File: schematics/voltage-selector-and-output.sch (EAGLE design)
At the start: 31 parts, among them IC1 5V, IC2 MIC2941, IC3 MCP41010P, IC5 12V, IC6 ATTINY85, Q1 2N3906

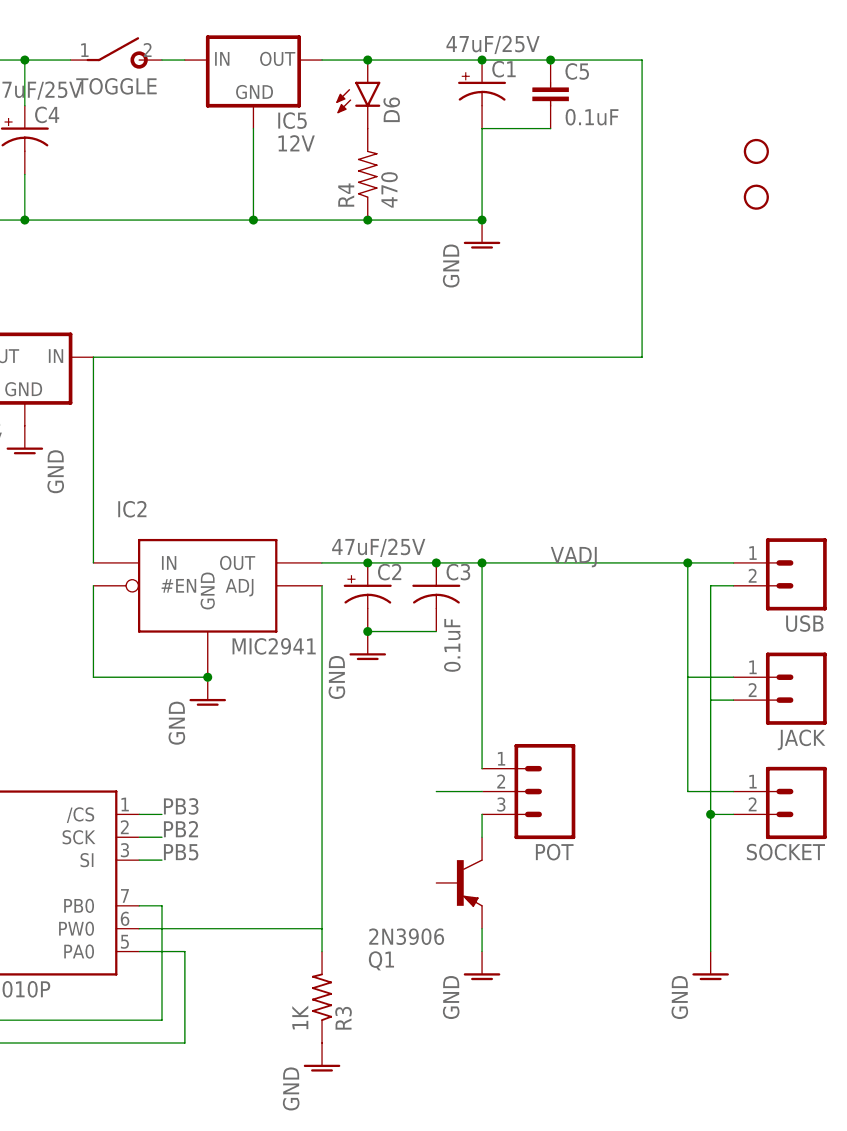
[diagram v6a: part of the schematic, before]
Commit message: Trying to deconflict the digi pot and register pins
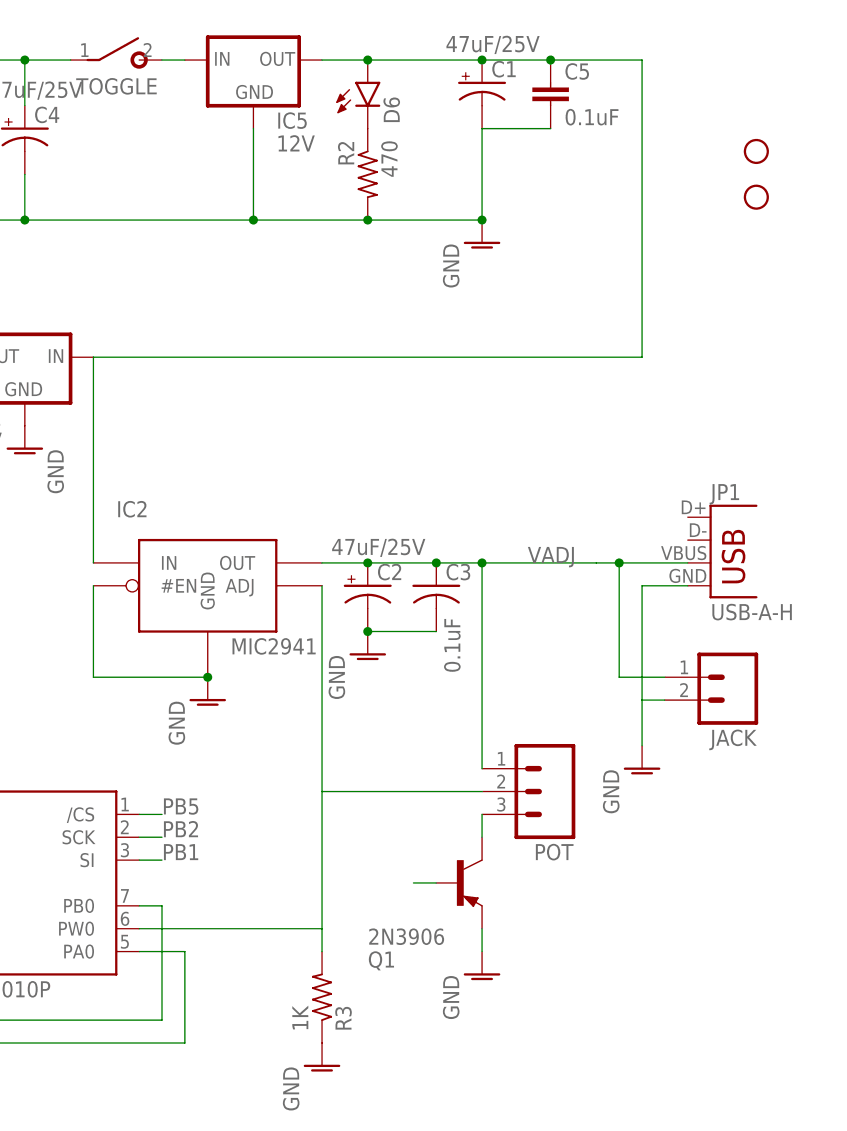
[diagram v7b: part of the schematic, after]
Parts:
- removed R4: 470, SparkFun-Resistors:RESISTORPTH-1/4W
- removed SOCKET, USB: (no value), SparkFun:M02PTH
- added JP1: USB-A-H, SparkFun-Connectors:USB-A-H
- added R2: 470, rcl-ez:R-US_0207/5V
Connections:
- new net N$8: Q1.B
- net AGND: now also JP1.GND, R2.2; no longer R4.1, SOCKET.2, USB.2
- net N$5: now also R2.1; no longer R4.2
- net PB1: now also IC3.SI
- net PB3: no longer IC3./CS
- net PB5: now also IC3./CS; no longer IC3.SI
- net VADJ: now also JP1.VBUS; no longer SOCKET.1, USB.1
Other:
- moved on the sheet: JACK
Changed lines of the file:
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@@
 <layer number="112" name="tSilk" color="7" fill="1" visible="yes" active="yes"/>
 <layer number="113" name="ReferenceLS" color="7" fill="1" visible="no" active="no"/>
+<layer number="114" name="Badge_Outline" color="7" fill="1" visible="yes" active="yes"/>
+<layer number="115" name="ReferenceISLANDS" color="7" fill="1" visible="yes" active="yes"/>
 <layer number="116" name="Patch_BOT" color="9" fill="4" visible="yes" active="yes"/>
 <layer number="118" name="Rect_Pads" color="7" fill="1" visible="no" active="no"/>
@@
 <part name="IC2" library="bbsup" deviceset="MIC2941" device=""/>
 <part name="IC6" library="SparkFun" deviceset="ATTINY13" device="DIP" value="ATTINY85"/>
-<part name="SOCKET" library="SparkFun" deviceset="M02" device="PTH"/>
 <part name="GND1" library="supply1" deviceset="AGND" device="" value="GND"/>
 <part name="GND2" library="supply1" deviceset="AGND" device="" value="GND"/>
@@
 <part name="IC1" library="v-reg" deviceset="78XXS" device="" value="5V"/>
 <part name="R1" library="rcl-ez" deviceset="R-US_" device="0207/5V" value="10k"/>
-<part name="USB" library="SparkFun" deviceset="M02" device="PTH"/>
 <part name="POT" library="SparkFun" deviceset="M03" device="PTH"/>
 <part name="GND11" library="supply1" deviceset="AGND" device="" value="GND"/>
@@
 <part name="C4" library="minimidi" deviceset="CPOL-US" device="E2.5-6" value="47uF/25V"/>
 <part name="XFRM" library="SparkFun" deviceset="M02" device="PTH"/>
-<part name="R4" library="SparkFun-Resistors" deviceset="RESISTOR" device="PTH-1/4W" value="470"/>
 <part name="D6" library="SparkFun-LED" deviceset="LED" device="-3MM-NO_SILK"/>
 <part name="C5" library="SparkFun-Capacitors" deviceset="CAP" device="PTH" value="0.1uF"/>
@@
 <part name="STANDOFF1" library="SparkFun-Electromechanical" deviceset="STAND-OFF" device=""/>
 <part name="STANDOFF2" library="SparkFun-Electromechanical" deviceset="STAND-OFF" device=""/>
+<part name="JP1" library="SparkFun-Connectors" deviceset="USB" device="-A-H"/>
+<part name="R2" library="rcl-ez" deviceset="R-US_" device="0207/5V" value="470"/>
 </parts>
 <sheets>
@@
 <instance part="IC2" gate="G$1" x="50.8" y="170.18"/>
 <instance part="IC6" gate="G$1" x="-20.32" y="177.8"/>
-<instance part="SOCKET" gate="G$1" x="116.84" y="147.32" rot="R180"/>
 <instance part="GND1" gate="VR1" x="50.8" y="157.48"/>
 <instance part="GND2" gate="VR1" x="68.58" y="162.56"/>
 <instance part="CLONE" gate="VR1" x="63.5" y="116.84"/>
-<instance part="GND4" gate="VR1" x="106.68" y="127"/>
+<instance part="GND4" gate="VR1" x="99.06" y="149.86"/>
 <instance part="GND5" gate="VR1" x="30.48" y="185.42" rot="MR0"/>
 <instance part="GND8" gate="VR1" x="2.54" y="200.66" rot="R180"/>
@@
 <instance part="IC1" gate="1" x="30.48" y="195.58" rot="MR0"/>
 <instance part="R1" gate="G$1" x="2.54" y="193.04" rot="MR270"/>
-<instance part="USB" gate="G$1" x="116.84" y="172.72" rot="R180"/>
 <instance part="POT" gate="G$1" x="88.9" y="147.32" rot="R180"/>
 <instance part="GND11" gate="VR1" x="81.28" y="127"/>
@@
 </instance>
 <instance part="XFRM" gate="G$1" x="-7.62" y="218.44"/>
-<instance part="R4" gate="G$1" x="68.58" y="215.9" rot="R90"/>
 <instance part="D6" gate="G$1" x="68.58" y="226.06"/>
 <instance part="C5" gate="G$1" x="88.9" y="223.52"/>
-<instance part="JACK" gate="G$1" x="116.84" y="160.02" rot="R180"/>
+<instance part="JACK" gate="G$1" x="109.22" y="160.02" rot="R180"/>
 <instance part="Q1" gate="G$1" x="78.74" y="137.16" rot="MR180"/>
 <instance part="C6" gate="G$1" x="-38.1" y="177.8"/>
@@
 <instance part="STANDOFF1" gate="G$1" x="111.76" y="218.44"/>
 <instance part="STANDOFF2" gate="G$1" x="111.76" y="213.36"/>
+<instance part="JP1" gate="G$1" x="106.68" y="170.18"/>
+<instance part="R2" gate="G$1" x="68.58" y="215.9" rot="MR270"/>
 </instances>
 <busses>
@@
 <pinref part="C3" gate="G$1" pin="1"/>
 <pinref part="IC2" gate="G$1" pin="OUT"/>
-<wire x1="81.28" y1="172.72" x2="104.14" y2="172.72" width="0.1524" layer="91"/>
-<wire x1="109.22" y1="172.72" x2="104.14" y2="172.72" width="0.1524" layer="91"/>
-<wire x1="104.14" y1="172.72" x2="104.14" y2="160.02" width="0.1524" layer="91"/>
-<pinref part="SOCKET" gate="G$1" pin="1"/>
-<wire x1="104.14" y1="147.32" x2="109.22" y2="147.32" width="0.1524" layer="91"/>
-<junction x="104.14" y="172.72"/>
+<wire x1="81.28" y1="172.72" x2="93.98" y2="172.72" width="0.1524" layer="91"/>
+<wire x1="96.52" y1="172.72" x2="96.52" y2="160.02" width="0.1524" layer="91"/>
+<junction x="96.52" y="172.72"/>
 <junction x="81.28" y="172.72"/>
-<pinref part="USB" gate="G$1" pin="1"/>
 <pinref part="POT" gate="G$1" pin="1"/>
 <pinref part="JACK" gate="G$1" pin="1"/>
-<wire x1="109.22" y1="160.02" x2="104.14" y2="160.02" width="0.1524" layer="91"/>
-<wire x1="104.14" y1="160.02" x2="104.14" y2="147.32" width="0.1524" layer="91"/>
-<label x="88.9" y="172.72" size="1.778" layer="95"/>
+<wire x1="101.6" y1="160.02" x2="96.52" y2="160.02" width="0.1524" layer="91"/>
+<label x="86.36" y="172.72" size="1.778" layer="95"/>
+<wire x1="104.14" y1="172.72" x2="93.98" y2="172.72" width="0.1524" layer="91"/>
+<pinref part="JP1" gate="G$1" pin="VBUS"/>
 </segment>
 <segment>
@@
 </segment>
 <segment>
-<pinref part="SOCKET" gate="G$1" pin="2"/>
-<wire x1="109.22" y1="144.78" x2="106.68" y2="144.78" width="0.1524" layer="91"/>
-<wire x1="106.68" y1="129.54" x2="106.68" y2="144.78" width="0.1524" layer="91"/>
-<wire x1="106.68" y1="144.78" x2="106.68" y2="157.48" width="0.1524" layer="91"/>
-<wire x1="106.68" y1="157.48" x2="106.68" y2="170.18" width="0.1524" layer="91"/>
-<wire x1="106.68" y1="170.18" x2="109.22" y2="170.18" width="0.1524" layer="91"/>
-<junction x="106.68" y="144.78"/>
+<wire x1="99.06" y1="152.4" x2="99.06" y2="157.48" width="0.1524" layer="91"/>
+<wire x1="99.06" y1="157.48" x2="99.06" y2="170.18" width="0.1524" layer="91"/>
+<wire x1="99.06" y1="170.18" x2="104.14" y2="170.18" width="0.1524" layer="91"/>
 <pinref part="GND4" gate="VR1" pin="AGND"/>
-<pinref part="USB" gate="G$1" pin="2"/>
 <pinref part="JACK" gate="G$1" pin="2"/>
-<wire x1="109.22" y1="157.48" x2="106.68" y2="157.48" width="0.1524" layer="91"/>
+<wire x1="101.6" y1="157.48" x2="99.06" y2="157.48" width="0.1524" layer="91"/>
+<pinref part="JP1" gate="G$1" pin="GND"/>
 </segment>
 <segment>
@@
 <wire x1="55.88" y1="220.98" x2="55.88" y2="210.82" width="0.1524" layer="91"/>
 <junction x="55.88" y="210.82"/>
-<pinref part="R4" gate="G$1" pin="1"/>
-<junction x="68.58" y="210.82"/>
 <pinref part="C5" gate="G$1" pin="2"/>
 <wire x1="88.9" y1="220.98" x2="81.28" y2="220.98" width="0.1524" layer="91"/>
+<pinref part="R2" gate="G$1" pin="2"/>
+<junction x="68.58" y="210.82"/>
 </segment>
 </net>
@@
 </segment>
 <segment>
-<pinref part="IC3" gate="P1" pin="SI"/>
-<wire x1="43.18" y1="139.7" x2="45.72" y2="139.7" width="0.1524" layer="91"/>
-<label x="45.72" y="139.7" size="1.778" layer="95"/>
+<pinref part="IC3" gate="P1" pin="/CS"/>
+<wire x1="43.18" y1="144.78" x2="45.72" y2="144.78" width="0.1524" layer="91"/>
+<label x="45.72" y="144.78" size="1.778" layer="95"/>
 </segment>
 </net>
@@
 <label x="-25.4" y="121.92" size="1.778" layer="95"/>
 </segment>
+<segment>
+<pinref part="IC3" gate="P1" pin="SI"/>
+<wire x1="43.18" y1="139.7" x2="45.72" y2="139.7" width="0.1524" layer="91"/>
+<label x="45.72" y="139.7" size="1.778" layer="95"/>
+</segment>
 </net>
 <net name="PB3" class="0">
@@
 <wire x1="-7.62" y1="177.8" x2="-5.08" y2="177.8" width="0.1524" layer="91"/>
 <label x="-5.08" y="177.8" size="1.778" layer="95"/>
-</segment>
-<segment>
-<pinref part="IC3" gate="P1" pin="/CS"/>
-<wire x1="43.18" y1="144.78" x2="45.72" y2="144.78" width="0.1524" layer="91"/>
-<label x="45.72" y="144.78" size="1.778" layer="95"/>
 </segment>
 <segment>
@@
 </segment>
 </net>
-<net name="N$5" class="0">
-<segment>
-<pinref part="R4" gate="G$1" pin="2"/>
-<pinref part="D6" gate="G$1" pin="C"/>
-</segment>
-</net>
 <net name="N$6" class="0">
 <segment>
 <pinref part="POT" gate="G$1" pin="2"/>
-<wire x1="81.28" y1="147.32" x2="76.2" y2="147.32" width="0.1524" layer="91"/>
+<wire x1="81.28" y1="147.32" x2="63.5" y2="147.32" width="0.1524" layer="91"/>
 </segment>
 </net>
@@
 </segment>
 </net>
+<net name="N$8" class="0">
+<segment>
+<pinref part="Q1" gate="G$1" pin="B"/>
+<wire x1="76.2" y1="137.16" x2="73.66" y2="137.16" width="0.1524" layer="91"/>
+</segment>
+</net>
+<net name="N$5" class="0">
+<segment>
+<pinref part="D6" gate="G$1" pin="C"/>
+<pinref part="R2" gate="G$1" pin="1"/>
+</segment>
+</net>

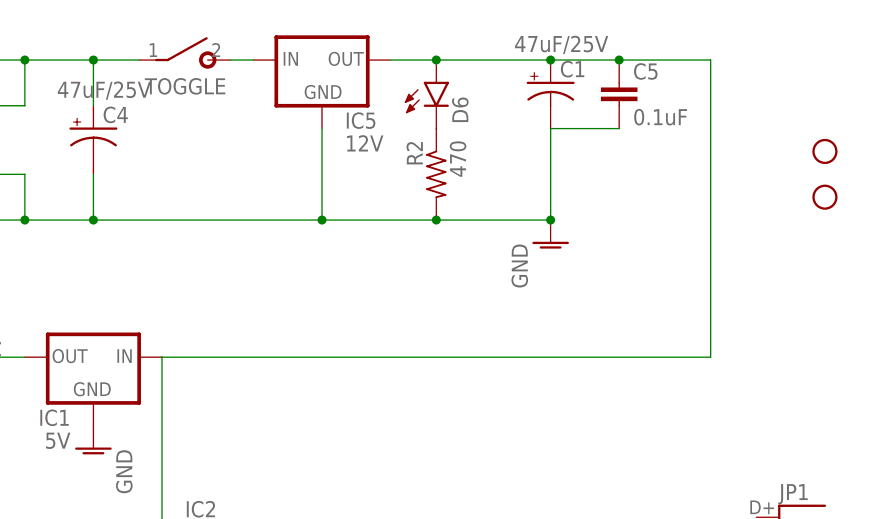
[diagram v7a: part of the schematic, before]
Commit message: LED was all wrong, of course
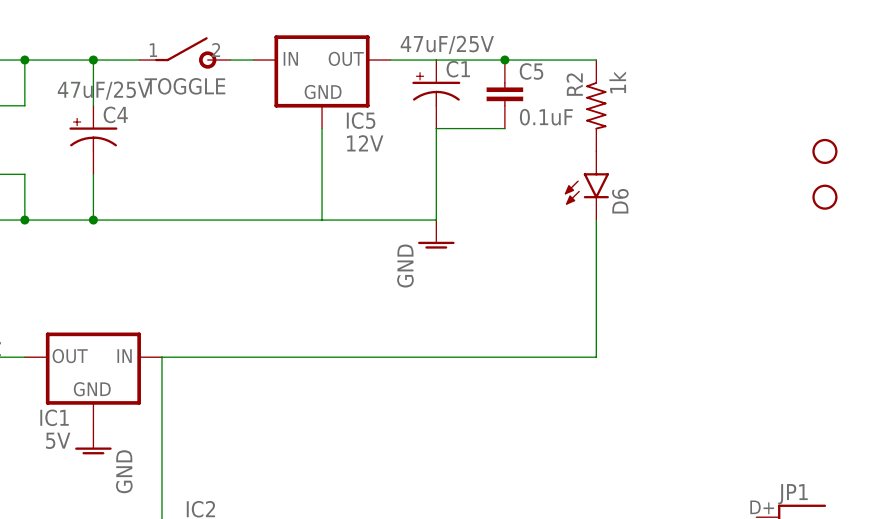
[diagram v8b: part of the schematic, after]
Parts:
- R2: value 470 -> 1k
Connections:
- new net N$10: D6.A, R2.2
- net AGND: no longer R2.2
- net N$5: now also C1.+, C5.1, IC5.OUT; no longer D6.C
- net RECTIFIED_12VCC: now also D6.C; no longer C1.+, C5.1, D6.A, IC5.OUT
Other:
- moved on the sheet: C1, C5, D6, R2
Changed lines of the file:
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@@
 <part name="STANDOFF2" library="SparkFun-Electromechanical" deviceset="STAND-OFF" device=""/>
 <part name="JP1" library="SparkFun-Connectors" deviceset="USB" device="-A-H"/>
-<part name="R2" library="rcl-ez" deviceset="R-US_" device="0207/5V" value="470"/>
+<part name="R2" library="rcl-ez" deviceset="R-US_" device="0207/5V" value="1k"/>
 </parts>
 <sheets>
@@
 <instance part="TOGGLE" gate="G$1" x="40.64" y="228.6" rot="R270"/>
 <instance part="D2" gate="1" x="15.24" y="223.52"/>
-<instance part="GND" gate="VR1" x="81.28" y="208.28"/>
-<instance part="C1" gate="G$1" x="81.28" y="226.06" smashed="yes">
-<attribute name="NAME" x="82.296" y="226.695" size="1.778" layer="95"/>
-<attribute name="VALUE" x="77.216" y="229.489" size="1.778" layer="96"/>
+<instance part="GND" gate="VR1" x="68.58" y="208.28"/>
+<instance part="C1" gate="G$1" x="68.58" y="226.06" smashed="yes">
+<attribute name="NAME" x="69.596" y="226.695" size="1.778" layer="95"/>
+<attribute name="VALUE" x="64.516" y="229.489" size="1.778" layer="96"/>
 </instance>
 <instance part="IC5" gate="1" x="55.88" y="228.6"/>
@@
 </instance>
 <instance part="XFRM" gate="G$1" x="-7.62" y="218.44"/>
-<instance part="D6" gate="G$1" x="68.58" y="226.06"/>
-<instance part="C5" gate="G$1" x="88.9" y="223.52"/>
+<instance part="D6" gate="G$1" x="86.36" y="215.9"/>
+<instance part="C5" gate="G$1" x="76.2" y="223.52"/>
 <instance part="JACK" gate="G$1" x="109.22" y="160.02" rot="R180"/>
 <instance part="Q1" gate="G$1" x="78.74" y="137.16" rot="MR180"/>
@@
 <instance part="STANDOFF2" gate="G$1" x="111.76" y="213.36"/>
 <instance part="JP1" gate="G$1" x="106.68" y="170.18"/>
-<instance part="R2" gate="G$1" x="68.58" y="215.9" rot="MR270"/>
+<instance part="R2" gate="G$1" x="86.36" y="223.52" rot="MR270"/>
 </instances>
 <busses>
@@
 <segment>
 <pinref part="GND" gate="VR1" pin="AGND"/>
+<pinref part="C1" gate="G$1" pin="-"/>
+<pinref part="C5" gate="G$1" pin="2"/>
+<wire x1="76.2" y1="220.98" x2="68.58" y2="220.98" width="0.1524" layer="91"/>
+<wire x1="68.58" y1="220.98" x2="68.58" y2="210.82" width="0.1524" layer="91"/>
 <wire x1="30.48" y1="210.82" x2="30.48" y2="215.9" width="0.1524" layer="91"/>
 <pinref part="D4" gate="1" pin="A"/>
@@
 <wire x1="30.48" y1="210.82" x2="55.88" y2="210.82" width="0.1524" layer="91"/>
 <junction x="30.48" y="210.82"/>
-<pinref part="C1" gate="G$1" pin="-"/>
-<wire x1="55.88" y1="210.82" x2="68.58" y2="210.82" width="0.1524" layer="91"/>
-<wire x1="68.58" y1="210.82" x2="81.28" y2="210.82" width="0.1524" layer="91"/>
-<wire x1="81.28" y1="220.98" x2="81.28" y2="210.82" width="0.1524" layer="91"/>
-<junction x="81.28" y="210.82"/>
 <pinref part="IC5" gate="1" pin="GND"/>
 <wire x1="55.88" y1="220.98" x2="55.88" y2="210.82" width="0.1524" layer="91"/>
-<junction x="55.88" y="210.82"/>
-<pinref part="C5" gate="G$1" pin="2"/>
-<wire x1="88.9" y1="220.98" x2="81.28" y2="220.98" width="0.1524" layer="91"/>
-<pinref part="R2" gate="G$1" pin="2"/>
-<junction x="68.58" y="210.82"/>
+<wire x1="55.88" y1="210.82" x2="68.58" y2="210.82" width="0.1524" layer="91"/>
 </segment>
 </net>
@@
 <pinref part="IC2" gate="G$1" pin="IN"/>
 <pinref part="IC1" gate="1" pin="IN"/>
-<pinref part="C1" gate="G$1" pin="+"/>
-<pinref part="IC5" gate="1" pin="OUT"/>
 <wire x1="38.1" y1="195.58" x2="38.1" y2="172.72" width="0.1524" layer="91"/>
-<wire x1="99.06" y1="228.6" x2="88.9" y2="228.6" width="0.1524" layer="91"/>
-<junction x="81.28" y="228.6"/>
-<wire x1="88.9" y1="228.6" x2="81.28" y2="228.6" width="0.1524" layer="91"/>
-<wire x1="63.5" y1="228.6" x2="68.58" y2="228.6" width="0.1524" layer="91"/>
-<wire x1="68.58" y1="228.6" x2="81.28" y2="228.6" width="0.1524" layer="91"/>
-<pinref part="D6" gate="G$1" pin="A"/>
-<junction x="68.58" y="228.6"/>
-<pinref part="C5" gate="G$1" pin="1"/>
-<junction x="88.9" y="228.6"/>
-<wire x1="99.06" y1="228.6" x2="99.06" y2="195.58" width="0.1524" layer="91"/>
-<wire x1="99.06" y1="195.58" x2="38.1" y2="195.58" width="0.1524" layer="91"/>
+<wire x1="86.36" y1="210.82" x2="86.36" y2="195.58" width="0.1524" layer="91"/>
+<wire x1="86.36" y1="195.58" x2="38.1" y2="195.58" width="0.1524" layer="91"/>
+<pinref part="D6" gate="G$1" pin="C"/>
 </segment>
 </net>
@@
 <net name="N$5" class="0">
 <segment>
-<pinref part="D6" gate="G$1" pin="C"/>
+<pinref part="IC5" gate="1" pin="OUT"/>
+<pinref part="C1" gate="G$1" pin="+"/>
 <pinref part="R2" gate="G$1" pin="1"/>
-</segment>
-</net>
+<wire x1="86.36" y1="228.6" x2="76.2" y2="228.6" width="0.1524" layer="91"/>
+<pinref part="C5" gate="G$1" pin="1"/>
+<junction x="76.2" y="228.6"/>
+<wire x1="76.2" y1="228.6" x2="68.58" y2="228.6" width="0.1524" layer="91"/>
+<wire x1="68.58" y1="228.6" x2="63.5" y2="228.6" width="0.1524" layer="91"/>
+</segment>
+</net>
+<net name="N$10" class="0">
+<segment>
+<pinref part="R2" gate="G$1" pin="2"/>
+<pinref part="D6" gate="G$1" pin="A"/>
+</segment>
+</net>
